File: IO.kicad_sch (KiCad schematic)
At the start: 17 parts, among them J11 C189893, J12 C265111, J3 C189893, J6 Connector, USB-TYPE-C-16P, U1 SP485EEN, U4 TJA1050T/CM,118, U6 USBLC6-2SC6

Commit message: added drv8353, stm32h723vgt6
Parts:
- removed JP1, JP2: 120R Load, Jumper:SolderJumper-2_P1.3mm_Open_TrianglePad1.0x1.5mm, symbol Jumper:SolderJumper_2_Open
- added SW1: SW_DIP_x02, symbol Switch:SW_DIP_x02
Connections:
- net CAN-: now also SW1.4
- net RS485+: now also SW1.2
- net at R8.1: now also SW1.3
- net at R22.1: now also SW1.1
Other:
- moved on the sheet: R8

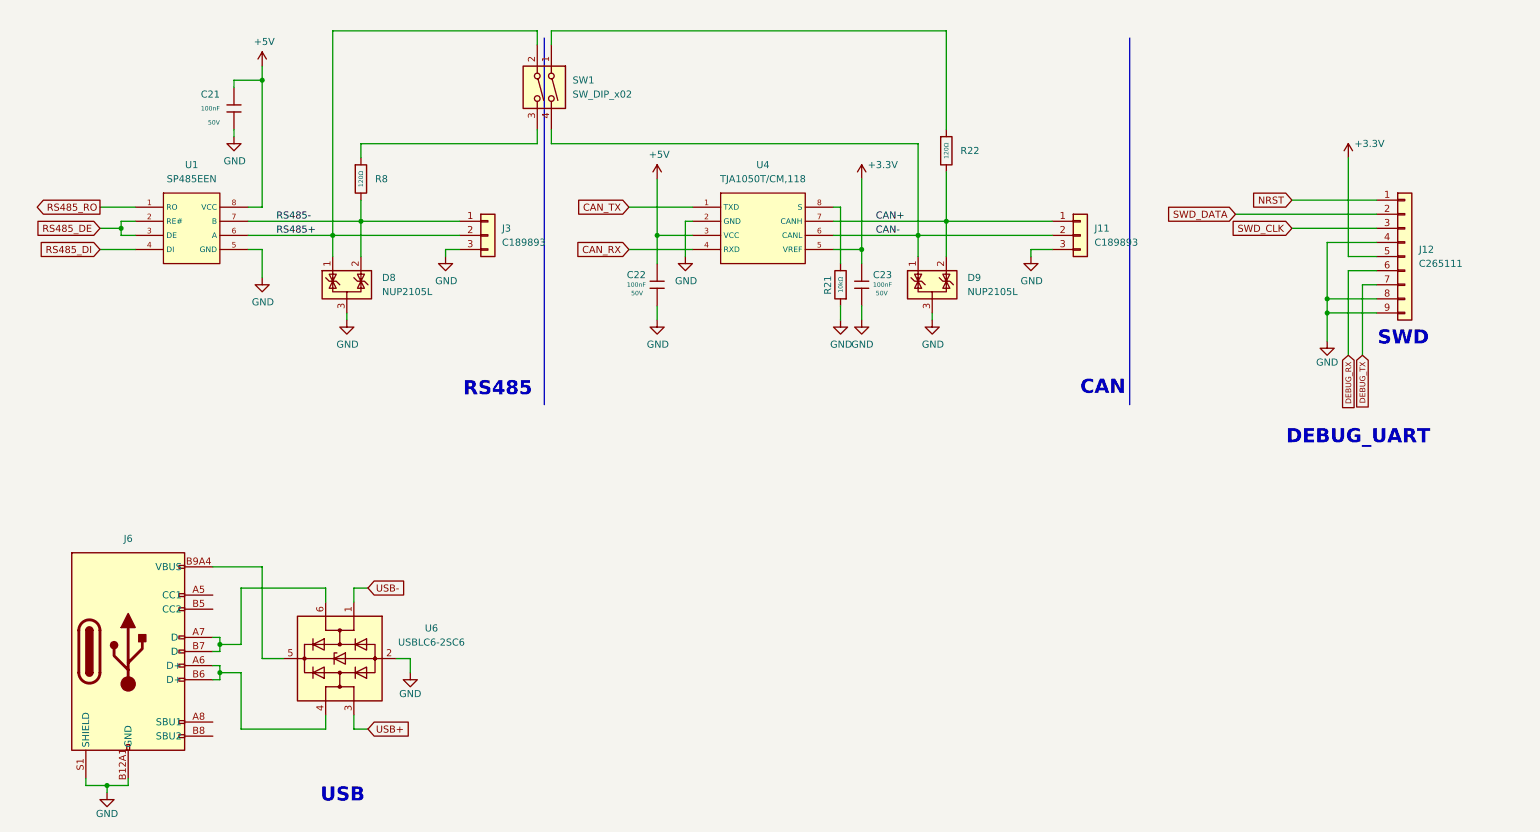
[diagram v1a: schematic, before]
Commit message: Circular pcb edge cut
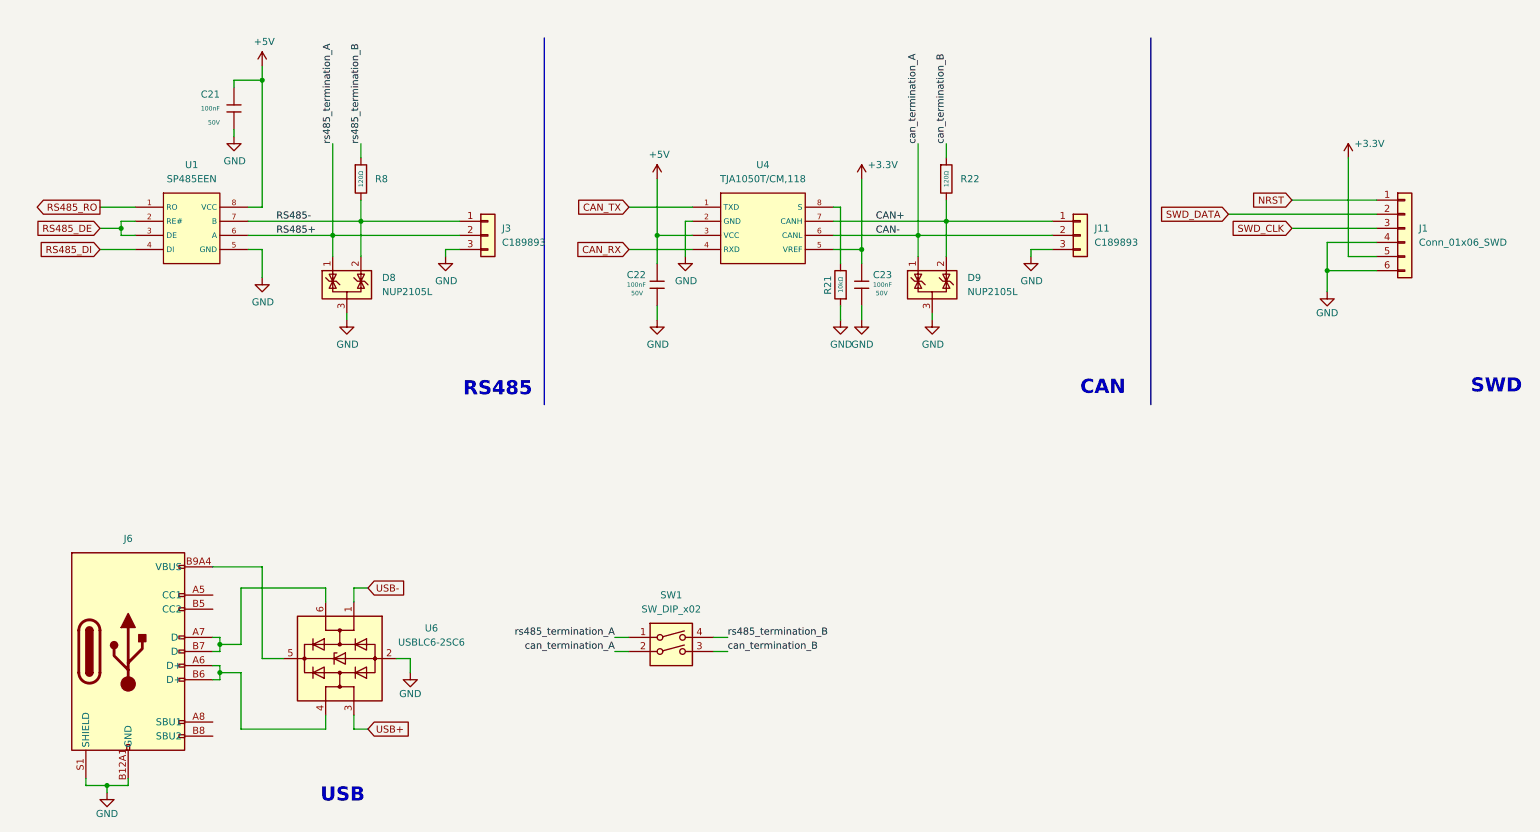
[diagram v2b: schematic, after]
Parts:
- removed J12: C265111, Connector_JST:JST_GH_SM08B-GHS-TB_1x08-1MP_P1.25mm_Horizontal, symbol Connector_Generic:Conn_01x09
- added J1: Conn_01x06_SWD, Connector_JST:JST_GH_SM05B-GHS-TB_1x05-1MP_P1.25mm_Horizontal, symbol Connector_Generic:Conn_01x06
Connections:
- net +3.3V: now also J1.5 (Pin_5)
- net CAN-: now also SW1.2; no longer SW1.4
- net GND: now also J1.4 (Pin_4), J1.6 (Pin_6)
- net NRST: now also J1.1 (Pin_1)
- net RS485+: now also SW1.1; no longer SW1.2
- net SWD_CLK: now also J1.3 (Pin_3)
- net SWD_DATA: now also J1.2 (Pin_2)
- net can_termination_B: now reaches SW1.3
- net can_termination_B: now also R22.1; no longer R8.1
- new net rs485_termination_B: R8.1, SW1.4
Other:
- note removed: "DEBUG_UART"
- moved on the sheet: R22, SW1

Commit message: Placement, some layout
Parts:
- SW1: footprint (none) -> Package_DIP:SMDIP-4_W7.62mm

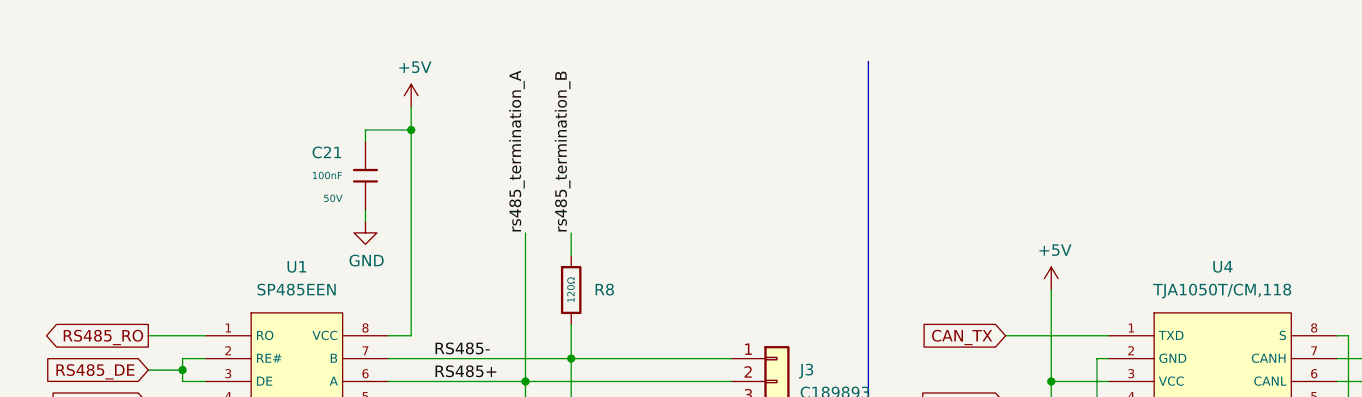
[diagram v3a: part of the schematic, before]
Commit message: More layout, add can,rs485 leds
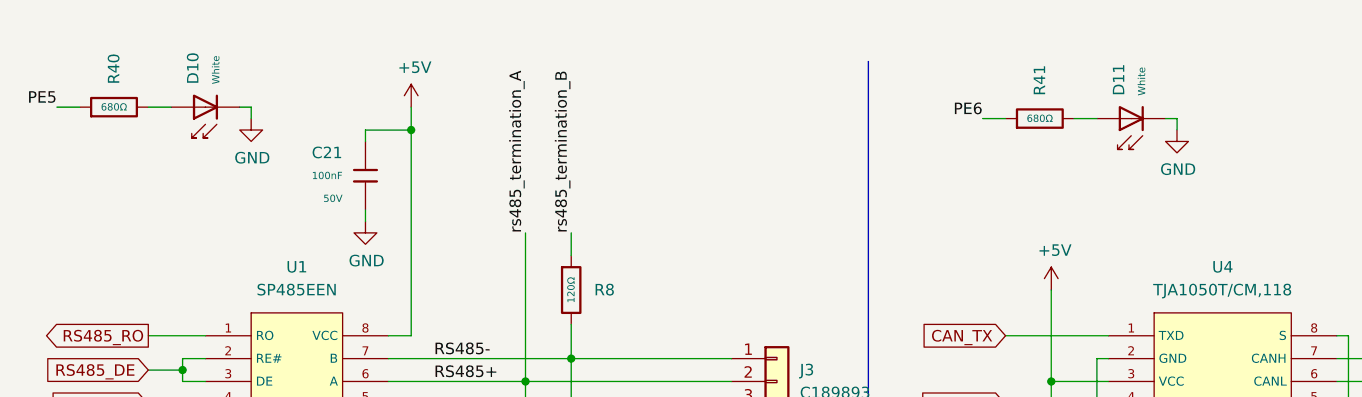
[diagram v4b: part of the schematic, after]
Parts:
- added D10, D11: White, PCM_JLCPCB:D_0603, symbol PCM_JLCPCB-Diodes:LED,0603,White
- added R40, R41: 680Ω, PCM_JLCPCB:R_0603, symbol PCM_JLCPCB-Resistors:0603,680Ω
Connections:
- net GND: now also D10.1, D11.1
- new net: D10.2, R40.2
- new net: D11.2, R41.2
- new net PE5: R40.1
- new net PE6: R41.1

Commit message: Layout 90%.
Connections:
- net PE5 renamed RS485_ACT
- net PE6 renamed CAN_ACT
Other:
- moved on the sheet: D10, D11, R40, R41

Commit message: DRC check - fine tuning
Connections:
- no-connect marks 0 -> 4
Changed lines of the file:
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@@
 		(color 0 0 0 0)
+	)
+	(no_connect
+		(at 48.26 119.38)
+	)
+	(no_connect
+		(at 48.26 142.24)
+	)
+	(no_connect
+		(at 48.26 139.7)
+	)
+	(no_connect
+		(at 48.26 116.84)
 	)
 	(wire
@@
 			(font
 				(size 1.27 1.27)
+				(color 255 116 0 1)
 			)
 			(justify right)
@@
 			(font
 				(size 1.27 1.27)
+				(color 255 116 0 1)
 			)
 			(justify right)
 		)
 		(property "Intersheetrefs" "${INTERSHEET_REFS}"
-			(at 16.0321 50.7206 0)
+			(at 15.4602 50.8 0)
 			(hide yes)
 			(show_name no)
@@
 			(font
 				(size 1.27 1.27)
+				(color 255 116 0 1)
 			)
 			(justify right)
 		)
 		(property "Intersheetrefs" "${INTERSHEET_REFS}"
-			(at 16.5764 54.5306 0)
+			(at 16.0044 54.61 0)
 			(hide yes)
 			(show_name no)

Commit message: Drc, Bom done
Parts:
- D8, D9: LCSC (none) -> C14486
- J11, J3: LCSC (none) -> C189893
- SW1: LCSC (none) -> C6331180
- U6: LCSC (none) -> C5261088
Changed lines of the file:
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@@
 			)
 		)
+		(property "LCSC" "C189893"
+			(at 207.01 50.7999 0)
+			(effects
+				(font
+					(size 1.27 1.27)
+				)
+				(hide yes)
+			)
+		)
 		(pin "1"
 		)
@@
 			)
 		)
+		(property "LCSC" "C5261088"
+			(at 87.63 122.8088 0)
+			(effects
+				(font
+					(size 1.27 1.27)
+				)
+				(hide yes)
+			)
+		)
 		(pin "1"
 		)
@@
 			)
 		)
+		(property "LCSC" "C14486"
+			(at 78.74 59.6899 0)
+			(effects
+				(font
+					(size 1.27 1.27)
+				)
+				(hide yes)
+			)
+		)
 		(pin "2"
 		)
@@
 			)
 		)
+		(property "LCSC" "C6331180"
+			(at 130.81 116.84 0)
+			(effects
+				(font
+					(size 1.27 1.27)
+				)
+				(hide yes)
+			)
+		)
 		(pin "3"
 		)
@@
 			)
 		)
+		(property "LCSC" "C189893"
+			(at 101.6 52.07 0)
+			(effects
+				(font
+					(size 1.27 1.27)
+				)
+				(hide yes)
+			)
+		)
 		(pin "1"
 		)
@@
 			)
 		)
+		(property "LCSC" "C14486"
+			(at 184.15 59.6899 0)
+			(effects
+				(font
+					(size 1.27 1.27)
+				)
+				(hide yes)
+			)
+		)
